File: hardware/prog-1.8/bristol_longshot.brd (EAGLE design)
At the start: 14 x 9 mm, 5 parts, among them IC3 TLV70018DCK

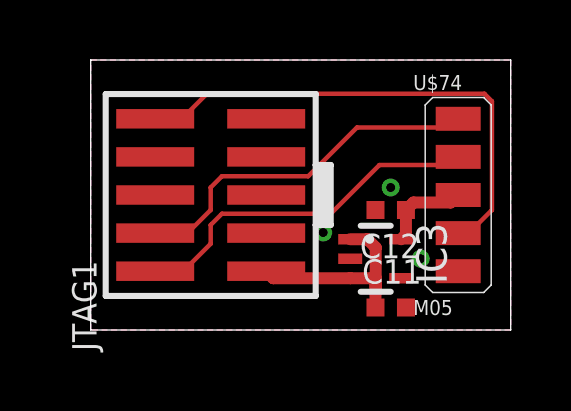
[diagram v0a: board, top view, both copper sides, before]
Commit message: Updated many parts lists, updated bard numbering, removed makefiles for inactive things
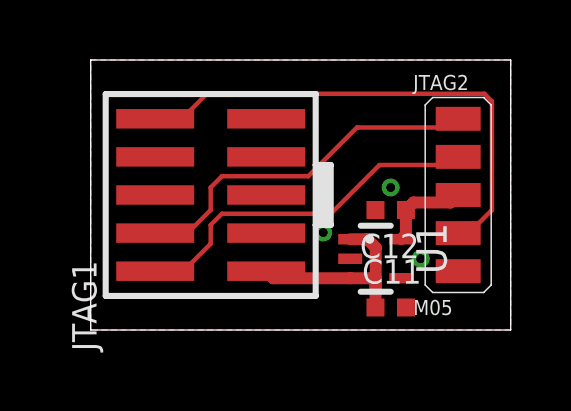
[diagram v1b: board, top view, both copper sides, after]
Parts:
- renumbered IC3 to U1, U$74 to JTAG2
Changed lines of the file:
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@@
 </autorouter>
 <elements>
-<element name="U$74" library="fbri" package="M05_SIDE" value="M05" x="12.25" y="4.5"/>
+<element name="JTAG2" library="fbri" package="M05_SIDE" value="M05" x="12.25" y="4.5"/>
 <element name="JTAG1" library="microbuilder_v3" package="2X05_1.27MM_SMT" value="" x="4" y="4.5" rot="R90"/>
-<element name="IC3" library="tlv700" package="SC70-5L" value="TLV70018DCK" x="9.5" y="2.375" rot="R270"/>
+<element name="U1" library="tlv700" package="SC70-5L" value="TLV70018DCK" x="9.5" y="2.375" rot="R270"/>
 <element name="C11" library="microbuilder_v3" package="_0402" value="1µF" x="10" y="0.75"/>
 <element name="C12" library="microbuilder_v3" package="_0402" value="1µF" x="10" y="4" rot="R180"/>
@@
 <vertex x="0" y="0"/>
 </polygon>
-<contactref element="U$74" pad="$1"/>
+<contactref element="JTAG2" pad="$1"/>
 <contactref element="JTAG1" pad="3"/>
 <contactref element="JTAG1" pad="5"/>
@@
 <via x="11" y="2.375" extent="1-16" drill="0.3"/>
 <contactref element="C11" pad="2"/>
-<contactref element="IC3" pad="2"/>
+<contactref element="U1" pad="2"/>
 <contactref element="C12" pad="2"/>
 <via x="10" y="4.75" extent="1-16" drill="0.3"/>
 </signal>
 <signal name="SWDIO">
-<contactref element="U$74" pad="$4"/>
+<contactref element="JTAG2" pad="$4"/>
 <contactref element="JTAG1" pad="2"/>
 <wire x1="2.15" y1="1.96" x2="3.085" y2="1.96" width="0.15" layer="1"/>
@@
 </signal>
 <signal name="SWDCLK">
-<contactref element="U$74" pad="$5"/>
+<contactref element="JTAG2" pad="$5"/>
 <contactref element="JTAG1" pad="4"/>
 <wire x1="2.15" y1="3.23" x2="3.23" y2="3.23" width="0.15" layer="1"/>
@@
 </signal>
 <signal name="EXT!RESET">
-<contactref element="U$74" pad="$2"/>
+<contactref element="JTAG2" pad="$2"/>
 <contactref element="JTAG1" pad="10"/>
 <wire x1="12.25" y1="3.23" x2="12.605" y2="3.23" width="0.15" layer="1"/>
@@
 <signal name="3.3V">
 <contactref element="JTAG1" pad="1"/>
-<contactref element="IC3" pad="1"/>
-<contactref element="IC3" pad="3"/>
+<contactref element="U1" pad="1"/>
+<contactref element="U1" pad="3"/>
 <contactref element="C11" pad="1"/>
 <wire x1="8.65" y1="1.725" x2="6.085" y2="1.725" width="0.4" layer="1"/>
@@
 </signal>
 <signal name="1.8V">
-<contactref element="IC3" pad="5"/>
+<contactref element="U1" pad="5"/>
 <contactref element="C12" pad="1"/>
-<contactref element="U$74" pad="$3"/>
+<contactref element="JTAG2" pad="$3"/>
 <wire x1="10.508" y1="4" x2="10.508" y2="3.183" width="0.4" layer="1"/>
 <wire x1="10.508" y1="3.183" x2="10.35" y2="3.025" width="0.4" layer="1"/>
